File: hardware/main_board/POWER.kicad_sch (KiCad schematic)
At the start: 8 parts, among them IC3 LM2937ET-3.3_NOPB, J11 UJC-H-G-SMT-1-P6-TR

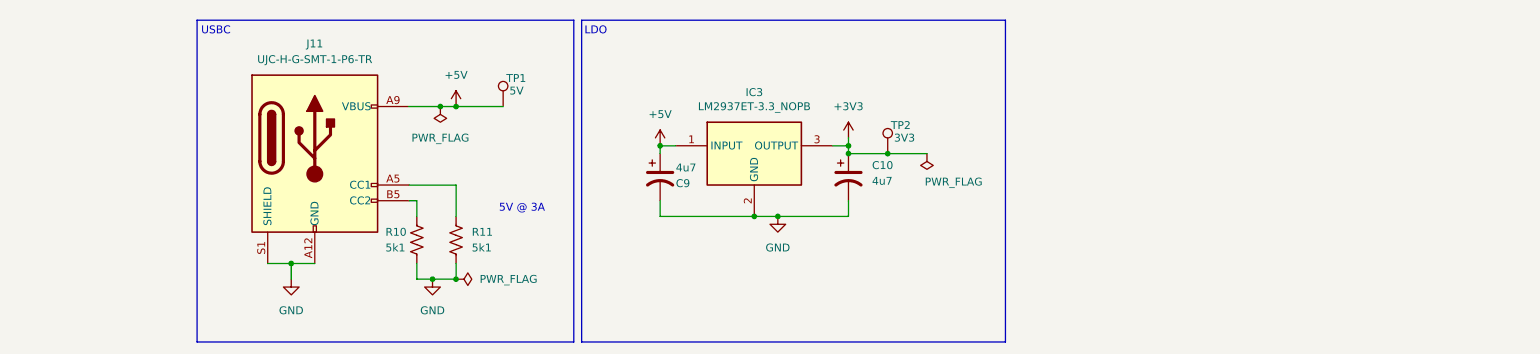
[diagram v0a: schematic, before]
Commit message: main board stuff. removed usbc for power. added level shifter for led logic signal. added lights for mux select signals. finished layout + pass DRC
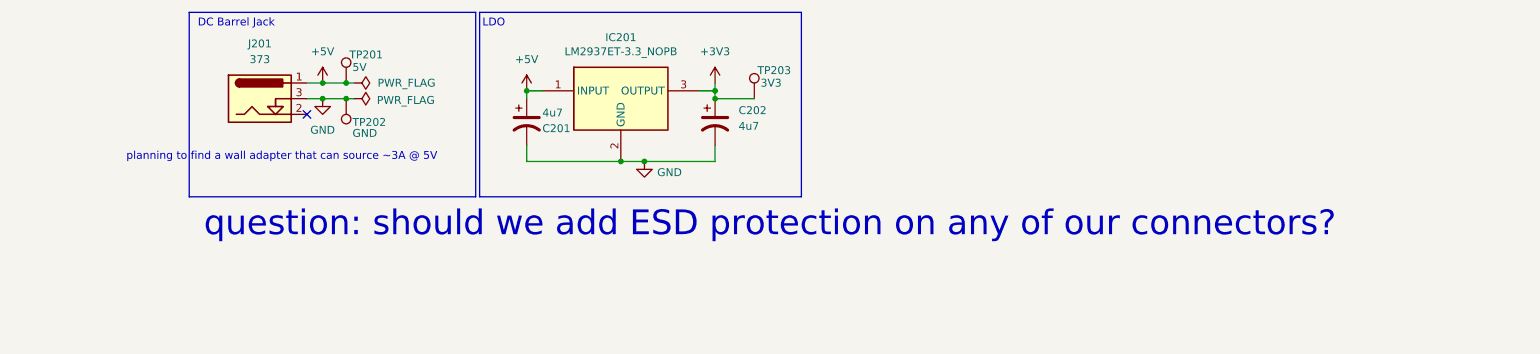
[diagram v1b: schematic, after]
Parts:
- removed J11: UJC-H-G-SMT-1-P6-TR, SamacSys_Parts:UJCHGSMT1P6TR, symbol Connector:USB_C_Receptacle_PowerOnly_6P
- removed R10, R11: 5k1, Resistor_SMD:R_0805_2012Metric, symbol Device:R_US
- added J201: 373, SamacSys_Parts:373, symbol SamacSys_Parts:Barrel_Jack
- added TP202: GND, SamacSys_Parts:bettertestpoint2, symbol Connector:TestPoint
- renumbered C9 to C201, C10 to C202, IC3 to IC201, TP1 to TP201, TP2 to TP203
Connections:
- net +5V: now also J201.1
- net GND: now also J201.3, TP202.1
- no-connect marks 0 -> 1
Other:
- note added: "DC Barrel Jack"
- note added: "planning to find a wall adapter that can source ~3A @ 5V"
- note added: "question: should we add ESD protection on any of our connectors?"
- note removed: "5V @ 3A"
- note removed: "USBC"
- moved on the sheet: C201, C202, IC201, TP201, TP203
